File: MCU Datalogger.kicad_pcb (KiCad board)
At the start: 2 copper layers, 51.6 x 30.2 mm, 29 parts, among them J1 Conn_01x04_Pin, J2 Conn_01x09_Pin, J3 Conn_01x04_Pin, J4 Conn_02x03_Odd_Even, U1 24LC1025, U2 24LC1025, U3 DS1337S_, U4 ATMEGA328P-AU, Y1 32.768 KHz, Y2 16 MHz

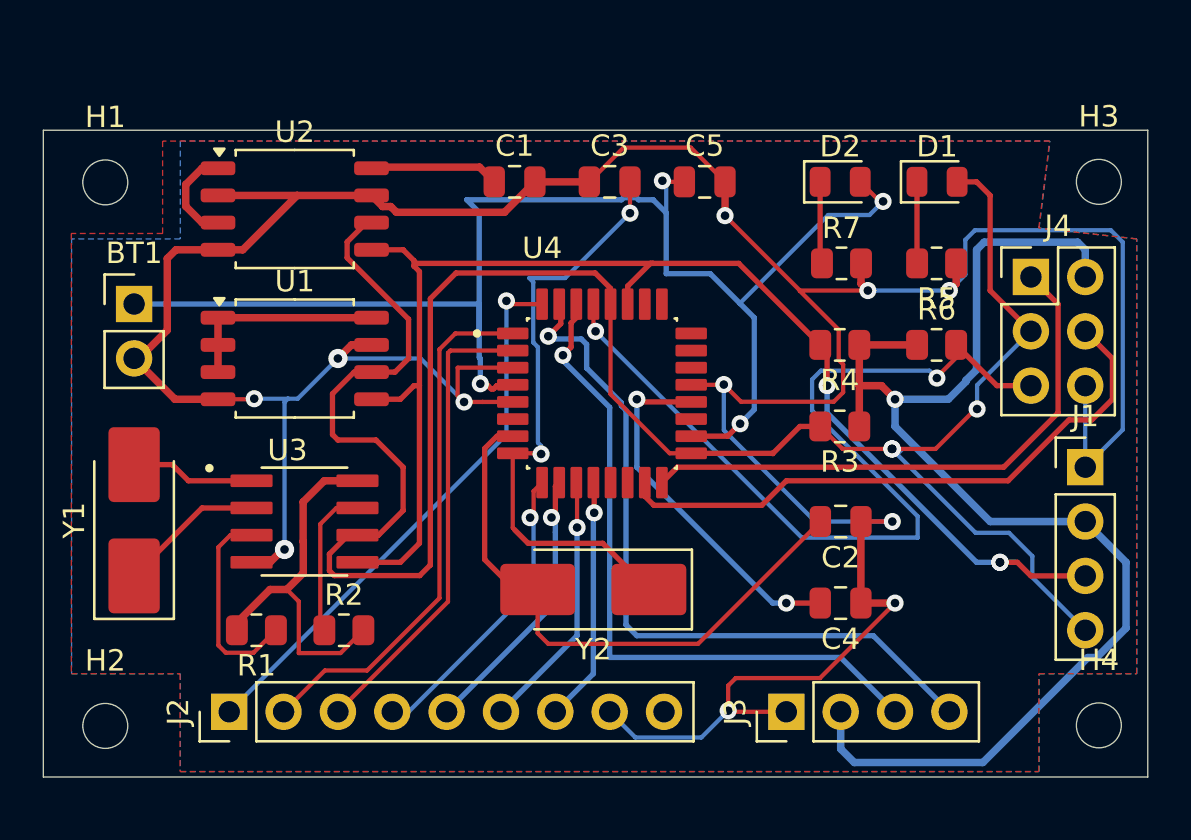
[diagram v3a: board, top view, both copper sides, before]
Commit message: Completed Routing.
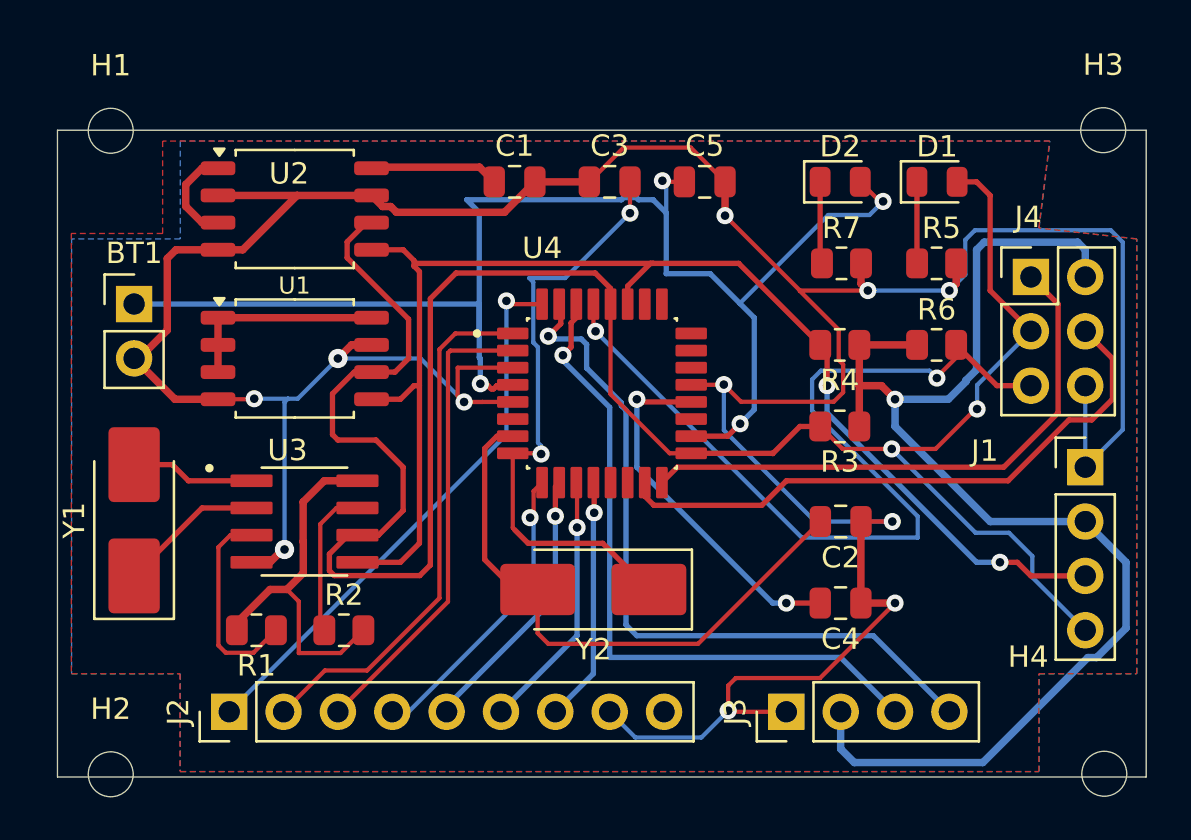
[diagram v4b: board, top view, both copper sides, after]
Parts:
- moved H1 2.43 mm to (66.9, 68.1)
- moved H3 2.42 mm to (113.2, 68.1)
- moved H2 2.27 mm to (66.9, 98.2)
- moved H4 2.27 mm to (113.3, 98.1)
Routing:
- net Net-(U4-PB6): track 28.5 -> 27.6 mm
- net /SDA: track 63.7 -> 62.9 mm, vias 3 -> 2
- net /D6: track 13.3 -> 12.6 mm
- net /SCK: track 103.7 -> 103.4 mm, vias 3 -> 2
- added copper zone on B.Cu, net GND
- removed copper zone on B.Cu, net (none)
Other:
- board size 51.6 x 30.2 mm -> 50.9 x 30.2 mm
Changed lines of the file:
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@@
 		(tags "Through hole pin header THT 1x04 2.54mm single row")
 		(property "Reference" "J1"
-			(at 0 -2.38 0)
+			(at -4.699 -0.762 0)
 			(layer "F.SilkS")
 			(effects
@@
 		(tags "resistor")
 		(property "Reference" "R5"
-			(at 0 -1.65 0)
+			(at -0.227064 1.651 0)
 			(layer "F.SilkS")
 			(effects
@@
 	(footprint "MountingHole:MountingHole_2.1mm"
 		(layer "F.Cu")
-		(at 66.5988 95.9104)
+		(at 66.8528 98.171)
 		(descr "Mounting Hole 2.1mm, no annular, generated by kicad-footprint-generator mountinghole.py")
 		(tags "mountinghole")
@@
 	(footprint "MountingHole:MountingHole_2.1mm"
 		(layer "F.Cu")
-		(at 113.03 95.885)
+		(at 113.284 98.1456)
 		(descr "Mounting Hole 2.1mm, no annular, generated by kicad-footprint-generator mountinghole.py")
 		(tags "mountinghole")
 		(property "Reference" "H4"
-			(at 0 -3.05 0)
+			(at -3.556 -5.461 0)
 			(layer "F.SilkS")
 			(effects
@@
 		(tags "Through hole pin header THT 2x03 2.54mm double row")
 		(property "Reference" "J4"
-			(at 1.27 -2.38 0)
+			(at -0.127 -2.794 0)
 			(layer "F.SilkS")
 			(effects
@@
 	(footprint "MountingHole:MountingHole_2.1mm"
 		(layer "F.Cu")
-		(at 66.5988 70.5104)
+		(at 66.8528 68.0974)
 		(descr "Mounting Hole 2.1mm, no annular, generated by kicad-footprint-generator mountinghole.py")
 		(tags "mountinghole")
@@
 	(footprint "MountingHole:MountingHole_2.1mm"
 		(layer "F.Cu")
-		(at 113.03 70.485)
+		(at 113.2332 68.072)
 		(descr "Mounting Hole 2.1mm, no annular, generated by kicad-footprint-generator mountinghole.py")
 		(tags "mountinghole")
@@
 		(tags "SOIC SO P-SOP SOP SOP-8 SO SO-8 8S2 S2AE/F K04-056 CASE-751BE SO8W 8-Pin-SOIC PSA W8-2 W8-4 W8MS-1 FPT-8P-M08")
 		(property "Reference" "U1"
-			(at 0 -3.6 0)
+			(at -0.0145 -3.4036 0)
 			(layer "F.SilkS")
 			(effects
 				(font
-					(size 1 1)
+					(size 0.8 0.8)
 					(thickness 0.15)
 				)
@@
 		(tags "SOIC SO P-SOP SOP SOP-8 SO SO-8 8S2 S2AE/F K04-056 CASE-751BE SO8W 8-Pin-SOIC PSA W8-2 W8-4 W8MS-1 FPT-8P-M08")
 		(property "Reference" "U2"
-			(at 0 -3.6 0)
+			(at -0.2685 -1.651 0)
 			(layer "F.SilkS")
 			(effects
@@
 	)
 	(gr_rect
-		(start 63.7032 68.072)
-		(end 115.316 98.298)
+		(start 64.3636 68.072)
+		(end 115.240201 98.298)
 		(stroke
 			(width 0.05)
@@
 	)
 	(segment
-		(start 77.47 78.74)
-		(end 77.571427 78.841427)
-		(width 0.35)
-		(layer "F.Cu")
-		(net 2)
-	)
-	(segment
 		(start 79.938268 71.639)
 		(end 80.206668 71.9074)
@@
 	)
 	(segment
-		(start 86.8025 89.535)
-		(end 86.8025 88.7075)
-		(width 0.25)
-		(layer "F.Cu")
-		(net 4)
-	)
-	(segment
 		(start 85.725 89.535)
 		(end 84.328 88.138)
@@
 	)
 	(segment
-		(start 85.725 83.255)
-		(end 85.64 83.17)
-		(width 0.25)
-		(layer "F.Cu")
-		(net 5)
-	)
-	(segment
-		(start 91.1098 71.9582)
-		(end 91.12 71.948)
-		(width 0.2)
-		(layer "F.Cu")
-		(net 5)
-	)
-	(segment
 		(start 86.7768 83.17)
 		(end 86.8172 83.2104)
@@
 	)
 	(segment
-		(start 103.3526 82.966)
-		(end 103.378 82.966)
-		(width 0.2)
-		(layer "F.Cu")
-		(net 7)
-	)
-	(segment
 		(start 78.802154 72.39)
 		(end 77.9015 73.290654)
@@
 	)
 	(segment
+		(start 105.4004 82.966)
+		(end 107.2642 81.1022)
+		(width 0.2)
+		(layer "F.Cu")
+		(net 7)
+	)
+	(segment
 		(start 81.788 75.946)
 		(end 82.988 74.746)
@@
 	)
 	(segment
+		(start 107.2642 81.1022)
+		(end 107.3404 81.1022)
+		(width 0.2)
+		(layer "F.Cu")
+		(net 7)
+	)
+	(segment
 		(start 78.3825 86.995)
 		(end 77.952624 86.995)
@@
 	)
 	(segment
+		(start 103.3526 82.966)
+		(end 105.4004 82.966)
+		(width 0.2)
+		(layer "F.Cu")
+		(net 7)
+	)
+	(segment
 		(start 107.95 71.12)
 		(end 107.315 70.485)
@@
 	)
 	(segment
-		(start 107.2642 81.1022)
-		(end 107.3404 81.1022)
-		(width 0.2)
-		(layer "F.Cu")
-		(net 7)
-	)
-	(segment
 		(start 93.98 83.17)
 		(end 92.973636 83.17)
@@
 	)
 	(segment
-		(start 103.378 82.966)
-		(end 105.4004 82.966)
-		(width 0.2)
-		(layer "F.Cu")
-		(net 7)
-	)
-	(segment
 		(start 77.0715 88.653876)
 		(end 77.303624 88.886)
@@
 	)
 	(segment
-		(start 105.4004 82.966)
-		(end 107.2642 81.1022)
-		(width 0.2)
-		(layer "F.Cu")
-		(net 7)
-	)
-	(segment
 		(start 81.788 88.392)
 		(end 81.788 75.946)
@@
 	)
 	(via
-		(at 103.378 82.966)
-		(size 0.8)
-		(drill 0.4)
-		(layers "F.Cu" "B.Cu")
-		(net 7)
-	)
-	(via
 		(at 103.3526 82.966)
 		(size 0.8)
@@
 	)
 	(segment
-		(start 103.6018 83.2152)
-		(end 103.831562 82.985438)
-		(width 0.2)
-		(layer "B.Cu")
-		(net 7)
-	)
-	(segment
 		(start 109.921 88.966)
 		(end 109.921 87.974636)
@@
 	)
 	(via
-		(at 108.4072 88.265)
-		(size 0.8)
-		(drill 0.4)
-		(layers "F.Cu" "B.Cu")
-		(net 10)
-	)
-	(via
 		(at 100.33 80.01)
 		(size 0.8)
@@
 	)
 	(segment
-		(start 109.22 88.265)
-		(end 107.315 88.265)
+		(start 100.33 81.28)
+		(end 100.33 80.01)
 		(width 0.25)
 		(layer "B.Cu")
@@
 	)
 	(segment
-		(start 100.33 81.28)
-		(end 100.33 80.01)
+		(start 107.315 88.265)
+		(end 108.4072 88.265)
 		(width 0.25)
 		(layer "B.Cu")
@@
 	)
 	(segment
-		(start 87.631403 84.718597)
-		(end 87.81 84.54)
-		(width 0.25)
-		(layer "F.Cu")
-		(net 13)
-	)
-	(segment
-		(start 87.449974 86.169869)
-		(end 87.631403 85.98844)
-		(width 0.25)
-		(layer "F.Cu")
-		(net 13)
-	)
-	(segment
-		(start 87.631403 85.98844)
+		(start 87.631403 86.106)
 		(end 87.631403 84.718597)
 		(width 0.25)
@@
 	)
 	(via
-		(at 87.449974 86.169869)
+		(at 87.631403 86.106)
 		(size 0.8)
 		(drill 0.4)
@@
 	)
 	(segment
-		(start 87.631403 86.869403)
-		(end 87.63 86.868)
+		(start 87.631403 89.916)
+		(end 82.55 94.997403)
 		(width 0.25)
 		(layer "B.Cu")
@@
 	)
 	(segment
-		(start 87.449974 86.169869)
-		(end 87.631403 86.351298)
-		(width 0.25)
-		(layer "B.Cu")
-		(net 13)
-	)
-	(segment
-		(start 87.631403 86.351298)
-		(end 87.631403 90.168597)
-		(width 0.25)
-		(layer "B.Cu")
-		(net 13)
-	)
-	(segment
-		(start 87.63 86.36)
-		(end 87.449974 86.179974)
-		(width 0.25)
-		(layer "B.Cu")
-		(net 13)
-	)
-	(segment
-		(start 87.631403 90.168597)
+		(start 82.55 94.997403)
 		(end 82.55 95.25)
 		(width 0.25)
@@
 	)
 	(segment
-		(start 87.449974 86.179974)
-		(end 87.449974 86.169869)
+		(start 87.631403 86.106)
+		(end 87.631403 89.916)
 		(width 0.25)
 		(layer "B.Cu")
@@
 	)
 	(segment
-		(start 87.051948 76.241948)
-		(end 87.01 76.2)
-		(width 0.25)
-		(layer "F.Cu")
-		(net 14)
-	)
-	(segment
 		(start 87.01 76.2)
 		(end 85.4964 76.2)
@@
 	)
 	(segment
-		(start 85.756 78.486)
-		(end 85.64 78.37)
-		(width 0.2)
-		(layer "F.Cu")
-		(net 17)
-	)
-	(segment
 		(start 82.615 90.105)
 		(end 82.615 78.4801)
@@
 	)
 	(segment
-		(start 77.47 95.25)
-		(end 77.47 95.006283)
-		(width 0.2)
-		(layer "B.Cu")
-		(net 17)
-	)
-	(segment
 		(start 88.3666 78.2066)
 		(end 88.3666 77.076066)
@@
 	)
 	(segment
-		(start 105.5624 79.502)
-		(end 105.4608 79.6036)
-		(width 0.2)
-		(layer "F.Cu")
-		(net 21)
-	)
-	(segment
-		(start 106.36 78.7044)
-		(end 105.5624 79.502)
+		(start 105.4608 79.6036)
+		(end 106.36 78.7044)
 		(width 0.2)
 		(layer "F.Cu")
@@
 			(thermal_gap 0.5)
 			(thermal_bridge_width 0.5)
-			(island_removal_mode 1)
-			(island_area_min 10)
 			(hatch_thickness 1)
 			(hatch_gap 1.5)
@@
 	)
 	(zone
-		(net 0)
-		(net_name "")
+		(net 2)
+		(net_name "GND")
 		(layer "B.Cu")
 		(hatch edge 0.5)
@@
 			(thermal_gap 0.5)
 			(thermal_bridge_width 0.5)
-			(island_removal_mode 1)
-			(island_area_min 10)
 			(hatch_thickness 1)
 			(hatch_gap 1.5)

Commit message: Refined Routing Completed
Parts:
- moved H1 0.80 mm to (66.5, 68.8)
- moved H3 0.78 mm to (113.0, 68.8)
- moved H2 0.70 mm to (66.5, 97.5)
- moved H4 0.70 mm to (113.0, 97.5)
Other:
- board size 50.9 x 30.2 mm -> 51.8 x 34.2 mm
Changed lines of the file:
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@@
 	(footprint "MountingHole:MountingHole_2.1mm"
 		(layer "F.Cu")
-		(at 66.8528 98.171)
+		(at 66.548 97.536)
 		(descr "Mounting Hole 2.1mm, no annular, generated by kicad-footprint-generator mountinghole.py")
 		(tags "mountinghole")
@@
 	(footprint "MountingHole:MountingHole_2.1mm"
 		(layer "F.Cu")
-		(at 113.284 98.1456)
+		(at 112.9792 97.5106)
 		(descr "Mounting Hole 2.1mm, no annular, generated by kicad-footprint-generator mountinghole.py")
 		(tags "mountinghole")
@@
 	(footprint "MountingHole:MountingHole_2.1mm"
 		(layer "F.Cu")
-		(at 66.8528 68.0974)
+		(at 66.548 68.834)
 		(descr "Mounting Hole 2.1mm, no annular, generated by kicad-footprint-generator mountinghole.py")
 		(tags "mountinghole")
 		(property "Reference" "H1"
-			(at 0 -3.05 0)
+			(at -0.928 3.866 0)
 			(layer "F.SilkS")
 			(effects
@@
 	(footprint "MountingHole:MountingHole_2.1mm"
 		(layer "F.Cu")
-		(at 113.2332 68.072)
+		(at 112.9792 68.8086)
 		(descr "Mounting Hole 2.1mm, no annular, generated by kicad-footprint-generator mountinghole.py")
 		(tags "mountinghole")
 		(property "Reference" "H3"
-			(at 0 -3.05 0)
+			(at -4.1592 0.8714 0)
 			(layer "F.SilkS")
 			(effects
@@
 		)
 	)
-	(gr_rect
-		(start 64.3636 68.072)
-		(end 115.240201 98.298)
+	(gr_line
+		(start 64.242154 96.219477)
+		(end 64.254954 70.341677)
+		(stroke
+			(width 0.05)
+			(type default)
+		)
+		(layer "Edge.Cuts")
+	)
+	(gr_arc
+		(start 64.254954 70.341677)
+		(mid 65.394627 66.437058)
+		(end 69.12 68.07)
+		(stroke
+			(width 0.05)
+			(type default)
+		)
+		(layer "Edge.Cuts")
+	)
+	(gr_arc
+		(start 69.17 98.29)
+		(mid 65.491502 100.145426)
+		(end 64.242152 96.219477)
+		(stroke
+			(width 0.05)
+			(type default)
+		)
+		(layer "Edge.Cuts")
+	)
+	(gr_line
+		(start 110.378307 98.305384)
+		(end 69.169999 98.29)
+		(stroke
+			(width 0.05)
+			(type default)
+		)
+		(layer "Edge.Cuts")
+	)
+	(gr_line
+		(start 115.316 70.2)
+		(end 115.32 96.190002)
+		(stroke
+			(width 0.05)
+			(type default)
+		)
+		(layer "Edge.Cuts")
+	)
+	(gr_line
+		(start 69.12 68.070003)
+		(end 110.396855 68.071052)
+		(stroke
+			(width 0.05)
+			(type default)
+		)
+		(layer "Edge.Cuts")
+	)
+	(gr_arc
+		(start 110.396855 68.071052)
+		(mid 114.051623 66.37391)
+		(end 115.316 70.2)
+		(stroke
+			(width 0.05)
+			(type default)
+		)
+		(layer "Edge.Cuts")
+	)
+	(gr_arc
+		(start 115.32 96.19)
+		(mid 114.034573 100.016923)
+		(end 110.378305 98.305384)
 		(stroke
 			(width 0.05)
 			(type default)
 		)
-		(fill no)
 		(layer "Edge.Cuts")
 	)
@@
 	)
 	(segment
-		(start 84.629801 80.159401)
-		(end 84.747221 80.159401)
+		(start 84.2148 80.01)
+		(end 85.6 80.01)
 		(width 0.25)
 		(layer "F.Cu")
@@
 	)
 	(segment
-		(start 84.4804 80.01)
-		(end 84.629801 80.159401)
-		(width 0.25)
-		(layer "F.Cu")
-		(net 1)
-	)
-	(segment
-		(start 84.2148 80.01)
-		(end 84.4804 80.01)
-		(width 0.25)
-		(layer "F.Cu")
-		(net 1)
-	)
-	(segment
-		(start 84.747221 80.159401)
-		(end 84.896622 80.01)
-		(width 0.25)
-		(layer "F.Cu")
-		(net 1)
-	)
-	(segment
 		(start 85.6 80.01)
 		(end 85.64 79.97)
@@
 	)
 	(segment
-		(start 84.896622 80.01)
-		(end 85.6 80.01)
-		(width 0.25)
-		(layer "F.Cu")
-		(net 1)
-	)
-	(segment
 		(start 92.6846 70.485)
 		(end 92.6338 70.4342)
@@
 	)
 	(segment
-		(start 90.932 91.186)
-		(end 91.44 91.694)
+		(start 87.4268 77.8256)
+		(end 88.83848 77.8256)
 		(width 0.25)
 		(layer "B.Cu")
@@
 	)
 	(segment
-		(start 87.2998 77.6986)
-		(end 87.4268 77.8256)
-		(width 0.25)
-		(layer "B.Cu")
-		(net 19)
-	)
-	(segment
-		(start 87.4268 77.8256)
-		(end 88.83848 77.8256)
+		(start 90.932 91.186)
+		(end 91.44 91.694)
 		(width 0.25)
 		(layer "B.Cu")
@@
 	)
 	(segment
-		(start 91.44 91.694)
-		(end 102.489 91.694)
+		(start 87.2998 77.6986)
+		(end 87.4268 77.8256)
 		(width 0.25)
 		(layer "B.Cu")
@@
 	)
 	(segment
-		(start 89.0926 79.18497)
-		(end 90.714 80.80637)
+		(start 102.489 91.694)
+		(end 106.045 95.25)
 		(width 0.25)
 		(layer "B.Cu")
@@
 	)
 	(segment
-		(start 102.489 91.694)
-		(end 106.045 95.25)
+		(start 90.932 81.16372)
+		(end 90.932 91.186)
 		(width 0.25)
 		(layer "B.Cu")
@@
 	)
 	(segment
-		(start 90.932 81.16372)
-		(end 90.932 91.186)
+		(start 91.44 91.694)
+		(end 102.489 91.694)
+		(width 0.25)
+		(layer "B.Cu")
+		(net 19)
+	)
+	(segment
+		(start 89.0926 79.18497)
+		(end 90.714 80.80637)
 		(width 0.25)
 		(layer "B.Cu")

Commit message: Version for manufacturing
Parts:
- added REF**: KiCad-Logo2_5mm_SilkScreen, Symbol:KiCad-Logo2_5mm_SilkScreen, B.Cu at (75.9, 72.2)
- moved H3 1.15 mm to (114.0, 68.2)
- moved H4 1.12 mm to (114.0, 98.1)
- moved H1 0.81 mm to (66.1, 68.2)
- moved H2 0.72 mm to (66.1, 98.1)
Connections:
- BT1 pad 1: Net-(BT1-+) -> /Vcc
- C5 pad 1: Net-(BT1-+) -> /Vcc
- D2 pad 2: Net-(BT1-+) -> /Vcc
- U4 pad 18: Net-(BT1-+) -> /Vcc
- U4 pad 4: Net-(BT1-+) -> /Vcc
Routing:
- net Net-(BT1-+): track 68.8 -> 0.00 mm, vias 4 -> 0
- net /Vcc: track 98.6 -> 164.9 mm, vias 1 -> 5
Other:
- board size 51.8 x 34.2 mm -> 53.8 x 35.8 mm
- board text added: "- 2Mbit EEPROM - RTC - I2C, SPI, GPIOs"
- board text added: "1"
- board text added: "2"
- board text added: "3"
- board text added: "4"
- board text added: "5"
- board text added: "6"
- board text added: "7"
- board text added: "Data Logger with ATMega328P"
- board text added: "GND"
- board text added: "GPIO"
- board text added: "I2C"
- board text added: "ICSP"
- board text added: "ICSP MISO | VCC SCK | MOSI RST | GND"
- board text added: "JP Electronics Oct-2025"
- board text added: "RX"
- board text added: "SCK"
- board text added: "SDA"
- board text added: "SERIAL"
- board text added: "TX"
- board text added: "VCC"

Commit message: Completed 2-layer PCB project
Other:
- board text added: "0.2000 mm / 0.0000 mm"
- board text added: "0.3000 mm"
- board text added: "1.6000 mm"
- board text added: "53.8097 mm x 35.8235 mm"
- board text added: "BOARD CHARACTERISTICS"
- board text added: "Board Thickness:"
- board text added: "Board overall dimensions:"
- board text added: "Castellated pads:"
- board text added: "Copper Finish:"
- board text added: "Copper Layer Count:"
- board text added: "Edge card connectors:"
- board text added: "Impedance Control:"
- board text added: "Min hole diameter:"
- board text added: "Min track/spacing:"
- board text added: "No"
- board text added: "None"
- board text added: "Plated Board Edge:"
